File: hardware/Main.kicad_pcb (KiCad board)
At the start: 2 copper layers, 54.5 x 57.5 mm, 34 parts, among them Q1 DMG2305UX, SW1 Bourns PEC11R, SW2 Bourns PEC11R, U1 LM386, U2 RDA5807M_Module, U3 RPi_Pico_TH, U4 S-1206B50-M3T1U

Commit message: Revised PCB Layout
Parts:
- AE1: footprint Package_TO_SOT_SMD:SOT-23-3 -> Connector_PinHeader_2.00mm:PinHeader_1x01_P2.00mm_Vertical; moved to F.Cu
- C1: footprint Capacitor_SMD:CP_Elec_8x10 -> Capacitor_Tantalum_SMD:CP_EIA-7343-30_AVX-N
- RV1: value R_Potentiometer_Trim_US -> 10kΩ
- moved LS1 52.1 mm to (165.0, 72.0), turned to 90 degrees
- moved AE1 42.8 mm to (142.5, 71.0), turned to 0 degrees
- moved C1 41.0 mm to (166.0, 76.0)
- moved C2 40.9 mm to (168.5, 81.5)
- moved C8 36.4 mm to (144.0, 109.9)
- moved R10 36.4 mm to (148.5, 109.8)
- moved R12 36.4 mm to (153.0, 109.9)
- moved R1 32.7 mm to (168.5, 87.9), turned to -90 degrees
- moved C6 27.9 mm to (144.0, 122.8)
- moved R6 27.9 mm to (148.5, 122.7)
- moved R8 27.9 mm to (153.0, 122.9)
- moved C3 25.6 mm to (159.6, 85.2), turned to 0 degrees
- moved C4 25.0 mm to (151.0, 86.5)
- moved R2 25.0 mm to (150.6, 90.5)
- moved R3 25.0 mm to (144.5, 93.0)
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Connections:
- RV1 pad 1: Net-(C4-Pad1) -> GND
- RV1 pad 2: GND -> Net-(U2-ROUT)
- RV1 pad 3: Net-(U2-ROUT) -> Net-(C4-Pad1)
- U3 pad 1: /ENC2A -> unconnected-(U3-GP0-Pad1)
- U3 pad 10: /DISP_DC -> unconnected-(U3-GP7-Pad10)
- U3 pad 15: unconnected-(U3-GP11-Pad15) -> /DISP_RES
- U3 pad 16: unconnected-(U3-GP12-Pad16) -> /DISP_DC
- U3 pad 17: unconnected-(U3-GP13-Pad17) -> /DISP_CS
- U3 pad 19: /ENC1A -> /DISP_SCLK
- U3 pad 2: /ENC2B -> unconnected-(U3-GP1-Pad2)
- U3 pad 20: /ENC1B -> /DISP_SDA
- U3 pad 21: /Radio-Audio/Radio_SDA -> /ENC1_BTN
- U3 pad 22: /Radio-Audio/Radio_SCL -> /ENC1A
- U3 pad 24: unconnected-(U3-GP18-Pad24) -> /ENC1B
- U3 pad 26: unconnected-(U3-GP20-Pad26) -> /ENC2_BTN
- U3 pad 27: /ENC1_BTN -> /ENC2A
- U3 pad 29: /ENC2_BTN -> /ENC2B
- U3 pad 31: unconnected-(U3-GP26/ADC0-Pad31) -> /Radio-Audio/Radio_SCL
- U3 pad 32: unconnected-(U3-GP27/ADC1-Pad32) -> /Radio-Audio/Radio_SDA
- U3 pad 4: /DISP_SCLK -> unconnected-(U3-GP2-Pad4)
- U3 pad 5: /DISP_SDA -> unconnected-(U3-GP3-Pad5)
- U3 pad 7: /DISP_CS -> unconnected-(U3-GP5-Pad7)
- U3 pad 9: /DISP_RES -> unconnected-(U3-GP6-Pad9)
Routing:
- net Net-(R6-Pad2): track 0.00 -> 28.0 mm
- net Net-(R10-Pad2): track 0.00 -> 27.9 mm
- net /DISP_RES: track 0.00 -> 27.1 mm
- net /ENC1_BTN: track 0.00 -> 23.4 mm
- net /ENC2_BTN: track 0.00 -> 22.1 mm
- net /DISP_DC: track 0.00 -> 20.0 mm
- net Net-(R11-Pad1): track 0.00 -> 17.0 mm
- net Net-(U1-+): track 0.00 -> 16.9 mm
- net Net-(R5-Pad1): track 0.00 -> 16.1 mm
- net /Radio-Audio/Radio_SCL: track 0.00 -> 14.3 mm
- net /DISP_CS: track 0.00 -> 14.0 mm
- net /DISP_SCLK: track 0.00 -> 13.5 mm
- net /Radio-Audio/Radio_SDA: track 0.00 -> 12.8 mm
- net Net-(AE1-A): track 0.00 -> 12.3 mm
- net /ENC2B: track 0.00 -> 12.2 mm
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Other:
- board size 54.5 x 57.5 mm -> 52 x 57 mm

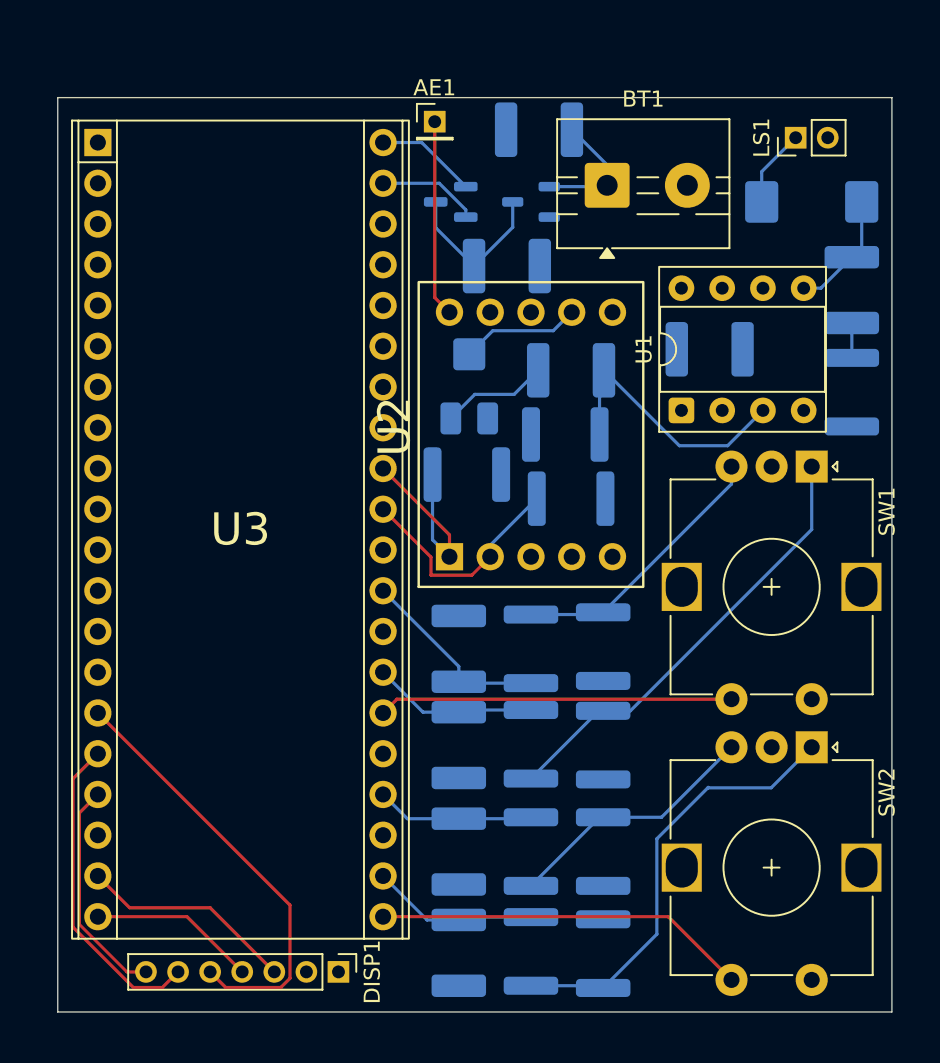
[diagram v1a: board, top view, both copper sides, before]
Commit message: Reduced Component Sizes + Added Mounting Holes
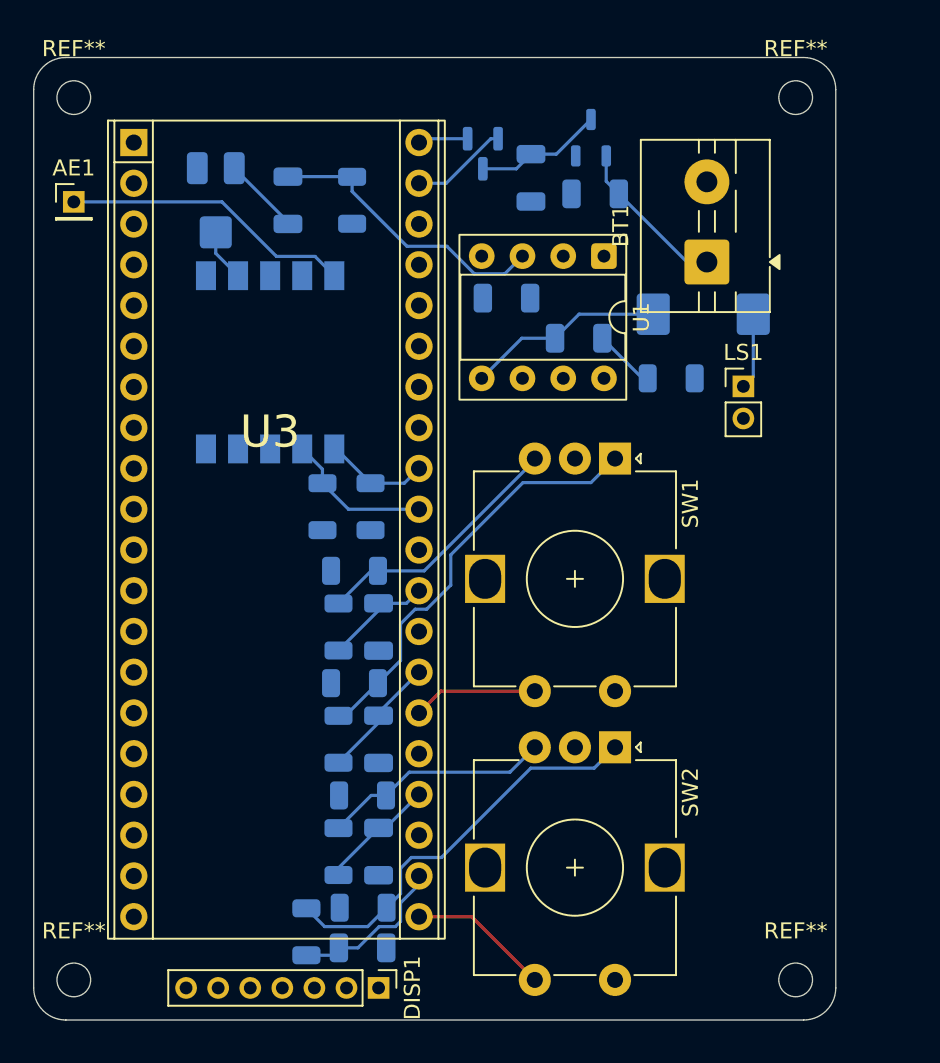
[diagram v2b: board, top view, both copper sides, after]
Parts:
- added REF**: MountingHole_2.1mm, MountingHole:MountingHole_2.1mm, F.Cu at (120.0, 124.5)
- added REF**: MountingHole_2.1mm, MountingHole:MountingHole_2.1mm, F.Cu at (120.0, 69.5)
- added REF**: MountingHole_2.1mm, MountingHole:MountingHole_2.1mm, F.Cu at (165.0, 69.5)
- added REF**: MountingHole_2.1mm, MountingHole:MountingHole_2.1mm, F.Cu at (165.0, 124.5)
- C10, C2, C3, C4, C5, C6, C7, C8, C9: footprint Capacitor_SMD:C_1812_4532Metric -> Capacitor_SMD:C_1206_3216Metric
- R1, R10, R11, R12, R2, R3, R4, R5, R6, R7, R8, R9: footprint Resistor_SMD:R_1812_4532Metric -> Resistor_SMD:R_1206_3216Metric
- U2: footprint ECE:RDA5807M_Module_TH -> ECE:RDA5807M_Module_SM; moved to B.Cu
- moved AE1 23.0 mm to (120.0, 76.0)
- moved C4 20.6 mm to (133.3, 75.9), turned to 90 degrees
- moved R2 19.7 mm to (137.3, 75.9), turned to -90 degrees
- moved RV1 19.6 mm to (128.8, 75.9), turned to 180 degrees
- moved C2 17.3 mm to (151.5, 84.5), turned to 0 degrees
- moved U2 16.9 mm to (132.2, 86.0)
- moved R11 16.2 mm to (137.5, 99.0), turned to 180 degrees
- moved R12 16.0 mm to (137.5, 106.0), turned to 180 degrees
- moved LS1 15.8 mm to (161.7, 87.5), turned to 0 degrees
- moved R4 15.5 mm to (135.5, 95.0), turned to 90 degrees
- moved R7 15.4 mm to (138.0, 113.0), turned to 180 degrees
- moved R8 15.2 mm to (138.0, 120.0), turned to 180 degrees
- moved R6 14.1 mm to (134.5, 121.5), turned to 90 degrees
- moved C3 13.1 mm to (147.0, 82.0), turned to 180 degrees
- moved SW1 12.3 mm to (153.7, 92.0)
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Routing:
- net /DISP_RES: track 27.1 -> 0.00 mm
- net /DISP_DC: track 20.0 -> 0.00 mm
- net /ENC1_BTN: track 23.4 -> 8.85 mm
- net /ENC2_BTN: track 22.1 -> 7.78 mm
- net /DISP_CS: track 14.0 -> 0.00 mm
- net /DISP_SCLK: track 13.5 -> 0.00 mm
- net /DISP_SDA: track 10.4 -> 0.00 mm
- net /Radio-Audio/Radio_SDA: track 12.8 -> 6.55 mm
- net Net-(AE1-A): track 12.3 -> 18.1 mm
- net /ENC2B: track 12.2 -> 6.82 mm
- net /Radio-Audio/Radio_SCL: track 14.3 -> 9.35 mm
- net Net-(C1-Pad1): track 7.51 -> 12.3 mm
- net Net-(U2-ROUT): track 7.48 -> 3.28 mm
- net /Power/VBUS: track 6.30 -> 3.13 mm
- net Net-(R6-Pad2): track 28.0 -> 25.3 mm
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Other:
- board size 52 x 57 mm -> 50 x 60 mm

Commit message: Repositioned + Added volume potentiometer to PMW Audio
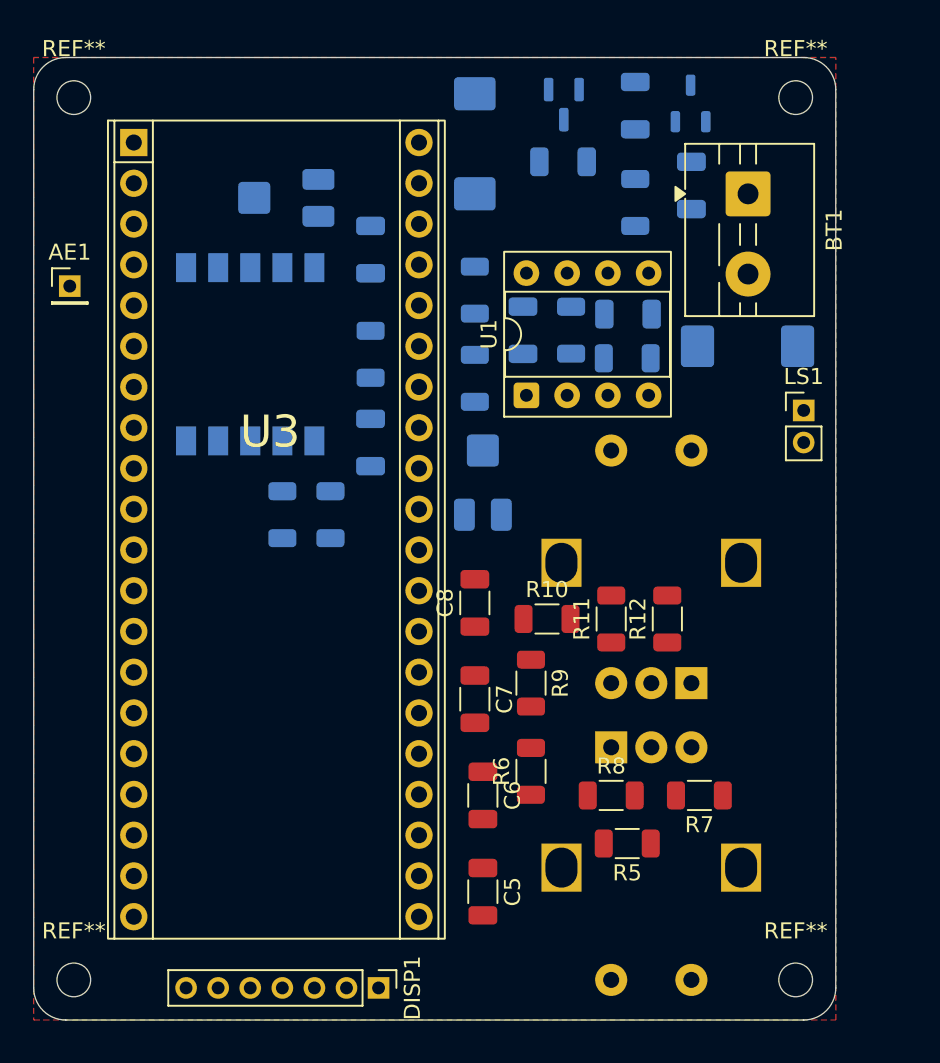
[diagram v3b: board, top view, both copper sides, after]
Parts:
- removed U2: RDA5807M_Module, ECE:RDA5807M_Module_SM
- added C11: 100nF, Capacitor_SMD:C_1206_3216Metric, B.Cu at (148.0, 84.0)
- added C12: 47uF, Capacitor_SMD:C_1206_3216Metric, B.Cu at (138.5, 91.0)
- added C13: 470 uF, Capacitor_Tantalum_SMD:CP_EIA-7343-30_AVX-N, B.Cu at (145.0, 72.4)
- added R13: 220, Resistor_SMD:R_1206_3216Metric, B.Cu at (138.5, 85.5)
- added R14: 100, Resistor_SMD:R_1206_3216Metric, B.Cu at (145.0, 81.5)
- added R15: 1.8k, Resistor_SMD:R_1206_3216Metric, B.Cu at (145.0, 87.0)
- added R16: No fit, Resistor_SMD:R_1206_3216Metric, B.Cu at (154.5, 85.8)
- added RV2: 10kΩ, Potentiometer_SMD:Potentiometer_Bourns_3314J_Vertical, B.Cu at (145.5, 93.5)
- added U5: RDA5807M_Module, ECE:RDA5807M_Module_SM, B.Cu at (131.0, 85.5)
- C5, C6, C7, C8, R10, R11, R12, R5, R6, R7, R8, R9: moved to F.Cu
- SW1, SW2: moved to B.Cu
- moved R7 21.0 mm to (159.0, 113.0)
- moved R12 19.9 mm to (157.0, 102.0), turned to 90 degrees
- moved R5 18.0 mm to (154.5, 116.0), turned to 180 degrees
- moved R6 17.2 mm to (148.5, 111.5)
- moved R8 17.0 mm to (153.5, 113.0), turned to 0 degrees
- moved R11 16.3 mm to (153.5, 102.0), turned to 90 degrees
- moved R2 15.9 mm to (151.0, 84.0), turned to 90 degrees
- moved R10 15.0 mm to (149.5, 102.0), turned to 0 degrees
- moved SW1 14.8 mm to (158.5, 106.0), turned to 90 degrees
- moved R9 12.5 mm to (148.5, 106.0)
- moved C6 12.1 mm to (145.5, 113.0), turned to -90 degrees
- moved R1 11.2 mm to (155.0, 76.0), turned to 90 degrees
- moved C8 10.4 mm to (145.0, 101.0), turned to 90 degrees
- moved U1 9.94 mm to (148.2, 88.1), turned to 90 degrees
- moved C3 9.20 mm to (150.5, 73.5)
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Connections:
- U3 pad 22: /ENC1A -> /ENC1B
- U3 pad 24: /ENC1B -> /ENC1A
- U3 pad 26: /ENC2_BTN -> /ENC2B
- U3 pad 29: /ENC2B -> /ENC2_BTN
- U3 pad 34: unconnected-(U3-GP28/ADC2-Pad34) -> /Radio-Audio/PWM Audio
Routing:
- net Net-(R10-Pad2): track 26.3 -> 0.00 mm
- net Net-(R6-Pad2): track 25.3 -> 0.00 mm
- net Net-(AE1-A): track 18.1 -> 0.00 mm
- net Net-(U1-+): track 18.1 -> 0.00 mm
- net Net-(R11-Pad1): track 16.0 -> 0.00 mm
- net Net-(R5-Pad1): track 14.3 -> 0.00 mm
- net Net-(C1-Pad1): track 12.3 -> 0.00 mm
- net /ENC1A: track 10.1 -> 0.00 mm
- net Net-(BT1-+): track 9.94 -> 0.00 mm
- net /Radio-Audio/Radio_SCL: track 9.35 -> 0.00 mm
- net /ENC1_BTN: track 8.85 -> 0.00 mm
- net Net-(Q1-D): track 8.01 -> 0.00 mm
- net /ENC2_BTN: track 7.78 -> 0.00 mm
- net /ENC2A: track 7.72 -> 0.00 mm
- net /ENC1B: track 7.36 -> 0.00 mm
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- added copper zone on F.Cu, net GND

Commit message: Did it all lmao (pcb traces ready for full review)
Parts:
- added R17: 0 ohm, Resistor_SMD:R_1206_3216Metric, B.Cu at (137.2, 81.0)
- added R18: 0 ohm, Resistor_SMD:R_1206_3216Metric, F.Cu at (120.0, 81.0)
- BT1: value 4.8-6V -> 4 AA
- LS1: footprint Connector_PinHeader_2.00mm:PinHeader_1x02_P2.00mm_Vertical -> TerminalBlock:TerminalBlock_MaiXu_MX126-5.0-02P_1x02_P5.00mm
- R11, R12, R7, R8: moved to B.Cu
- moved R14 36.7 mm to (129.0, 114.5), turned to 0 degrees
- moved C11 33.4 mm to (129.0, 111.5), turned to 0 degrees
- moved R15 29.7 mm to (135.8, 115.2), turned to 0 degrees
- moved C3 27.0 mm to (146.5, 100.2), turned to -90 degrees
- moved R9 26.0 mm to (149.8, 80.0), turned to 0 degrees
- moved C7 25.2 mm to (152.8, 83.0), turned to 180 degrees
- moved R16 25.1 mm to (135.8, 102.5)
- moved R13 24.9 mm to (129.0, 108.5), turned to 180 degrees
- moved R1 24.7 mm to (150.0, 100.2), turned to -90 degrees
- moved C12 21.7 mm to (135.8, 112.5), turned to 180 degrees
- moved R11 20.8 mm to (145.0, 83.0), turned to -90 degrees
- moved SW1 20.7 mm to (148.2, 88.0), turned to 0 degrees
- moved R12 18.4 mm to (145.0, 88.0)
- moved C2 17.3 mm to (153.0, 100.2), turned to -90 degrees
- moved RV2 17.1 mm to (135.8, 107.5), turned to 180 degrees
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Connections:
- C4 pad 2: Net-(U1-+) -> Net-(C4-Pad2)
- R2 pad 1: Net-(U1-+) -> Net-(C4-Pad2)
- U3 pad 11: unconnected-(U3-GP8-Pad11) -> /Radio-Audio/Radio_SDA
- U3 pad 12: unconnected-(U3-GP9-Pad12) -> /Radio-Audio/Radio_SCL
- U3 pad 14: unconnected-(U3-GP10-Pad14) -> /Radio-Audio/PWM Audio
- U3 pad 26: /ENC2B -> unconnected-(U3-GP20-Pad26)
- U3 pad 27: /ENC2A -> unconnected-(U3-GP21-Pad27)
- U3 pad 29: /ENC2_BTN -> unconnected-(U3-GP22-Pad29)
- U3 pad 31: /Radio-Audio/Radio_SCL -> /ENC2B
- U3 pad 32: /Radio-Audio/Radio_SDA -> /ENC2A
- U3 pad 34: /Radio-Audio/PWM Audio -> /ENC2_BTN
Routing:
- net +3.3V: track 0.00 -> 73.0 mm, vias 0 -> 4
- net Net-(U1-+): track 0.00 -> 51.5 mm
- net GND: track 0.00 -> 46.8 mm, vias 0 -> 14
- net +5V: track 0.00 -> 46.3 mm
- net Net-(AE1-A): track 0.00 -> 32.9 mm
- net /ENC1_BTN: track 0.00 -> 29.0 mm
- net /ENC2B: track 0.00 -> 27.3 mm
- net /ENC2_BTN: track 0.00 -> 25.5 mm
- net /Radio-Audio/Radio_SDA: track 0.00 -> 23.6 mm
- net /ENC1B: track 0.00 -> 22.7 mm
- net /ENC1A: track 0.00 -> 22.2 mm, vias 0 -> 1
- net /DISP_RES: track 0.00 -> 19.5 mm
- net /DISP_DC: track 0.00 -> 16.2 mm
- net Net-(BT1-+): track 0.00 -> 14.9 mm
- net /ENC2A: track 0.00 -> 14.6 mm
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- added copper zone on F.Cu, net /Radio-Audio/Board Antenna
- added copper zone on B.Cu, net GND

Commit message: done for real this time
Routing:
- net GND: track 46.8 -> 45.1 mm
- net +5V: track 46.3 -> 47.8 mm
- net Net-(Q1-D): track 12.3 -> 11.3 mm

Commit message: PCB tweaks
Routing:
- net /ENC2B: track 27.3 -> 32.6 mm
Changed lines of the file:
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@@
 		(tags "resistor")
 		(property "Reference" "R18"
-			(at 0 -1.83 90)
+			(at 3.0625 0 180)
 			(layer "F.SilkS")
 			(effects
@@
 		)
 		(property "Value" "0.01uF"
-			(at 0 1.85 0)
+			(at -5.05 0 0)
 			(layer "F.Fab")
 			(effects
@@
 			(at 0 -3.05 0)
 			(layer "F.SilkS")
+			(hide yes)
 			(effects
 				(font
@@
 		)
 		(property "Value" "10kΩ"
-			(at 0 1.83 0)
+			(at 4.15 -0.1 0)
 			(layer "F.Fab")
 			(effects
@@
 			(at 0 -3.05 0)
 			(layer "F.SilkS")
+			(hide yes)
 			(effects
 				(font
@@
 			(at 2.24 3.05 0)
 			(layer "F.Fab")
+			(hide yes)
 			(effects
 				(font
@@
 			(layer "F.CrtYd")
 		)
-		(fp_text user "${REFERENCE}"
-			(at 0 0 0)
-			(layer "F.Fab")
-			(effects
-				(font
-					(size 1 1)
-					(thickness 0.15)
-				)
-			)
-		)
 		(pad "" np_thru_hole circle
 			(at 0 0)
@@
 		)
 		(property "Value" "10kΩ"
-			(at 0 1.83 0)
+			(at -4.15 -0.1 0)
 			(layer "F.Fab")
 			(effects
@@
 		(tags "Through hole pin header THT 1x07 2.00mm single row")
 		(property "Reference" "DISP1"
-			(at 0 -2.11 90)
+			(at 0 -3.75 180)
 			(layer "F.SilkS")
 			(effects
@@
 		(tags "mountinghole")
 		(property "Reference" "REF**"
-			(at 0 -3.05 0)
+			(at -0.4 4.5 0)
 			(layer "F.SilkS")
+			(hide yes)
 			(effects
 				(font
@@
 		)
 		(property "Value" "MountingHole_2.1mm"
-			(at 2.24 3.05 0)
+			(at 11.3 6.9 0)
 			(layer "F.Fab")
+			(hide yes)
 			(effects
 				(font
@@
 			(layer "F.CrtYd")
 		)
-		(fp_text user "${REFERENCE}"
-			(at 0 0 0)
-			(layer "F.Fab")
-			(effects
-				(font
-					(size 1 1)
-					(thickness 0.15)
-				)
-			)
-		)
 		(pad "" np_thru_hole circle
 			(at 0 0)
@@
 		(tags "THT terminal block MaiXu MX126-5.0-02P pitch 5mm size 10.5x7.8mm drill 1.3mm pad 2.8mm")
 		(property "Reference" "LS1"
-			(at 2.25 -5.12 90)
+			(at -4.05 0.0325 180)
 			(layer "F.SilkS")
 			(effects
@@
 			(at 0 -3.05 0)
 			(layer "F.SilkS")
+			(hide yes)
 			(effects
 				(font
@@
 		)
 		(property "Value" "0.01uF"
-			(at 0 1.85 0)
+			(at -4.65 -0.1 0)
 			(layer "F.Fab")
 			(effects
@@
 			(at 9.64619 -2.4 0)
 			(layer "F.Fab")
+			(hide yes)
 			(effects
 				(font
@@
 	)
 	(segment
+		(start 128.85 115.8125)
+		(end 127.5375 114.5)
+		(width 0.35)
+		(layer "B.Cu")
+		(net 3)
+	)
+	(segment
 		(start 146.8875 72.7)
 		(end 148.05 72.7)
@@
 	)
 	(segment
-		(start 134.2875 115.25)
-		(end 133.725 115.8125)
+		(start 133.725 115.8125)
+		(end 128.85 115.8125)
 		(width 0.35)
 		(layer "B.Cu")
@@
 	)
 	(segment
-		(start 128.85 115.8125)
-		(end 127.5375 114.5)
-		(width 0.35)
-		(layer "B.Cu")
-		(net 3)
-	)
-	(segment
 		(start 129.025 107.475)
 		(end 128.55 107)
@@
 	)
 	(segment
+		(start 134.2875 115.25)
+		(end 133.725 115.8125)
+		(width 0.35)
+		(layer "B.Cu")
+		(net 3)
+	)
+	(segment
 		(start 140.275 69.5)
 		(end 139.225 69.5)
@@
 	)
 	(segment
-		(start 133.725 115.8125)
-		(end 128.85 115.8125)
-		(width 0.35)
-		(layer "B.Cu")
-		(net 3)
-	)
-	(segment
 		(start 137.85 105.5)
 		(end 137.9 105.45)
@@
 	)
 	(segment
-		(start 151.2125 80)
-		(end 154.2125 83)
+		(start 157.8 92.402)
+		(end 155.042 95.16)
 		(width 0.2)
 		(layer "F.Cu")
@@
 	)
 	(segment
-		(start 153.66484 89.201)
-		(end 153.66484 90.27132)
+		(start 151.2125 80)
+		(end 154.2125 83)
 		(width 0.2)
 		(layer "F.Cu")
@@
 	)
 	(segment
-		(start 155.101 88.88516)
-		(end 154.78516 89.201)
+		(start 157.8 86.575)
+		(end 157.8 92.402)
 		(width 0.2)
 		(layer "F.Cu")
@@
 	)
 	(segment
-		(start 148.77616 95.16)
+		(start 155.042 95.16)
 		(end 141.52 95.16)
 		(width 0.2)
@@
 	(segment
 		(start 154.225 83)
-		(end 155.101 83.876)
-		(width 0.2)
-		(layer "F.Cu")
-		(net 12)
-	)
-	(segment
-		(start 153.66484 90.27132)
-		(end 148.77616 95.16)
-		(width 0.2)
-		(layer "F.Cu")
-		(net 12)
-	)
-	(segment
-		(start 154.78516 89.201)
-		(end 153.66484 89.201)
-		(width 0.2)
-		(layer "F.Cu")
-		(net 12)
-	)
-	(segment
-		(start 155.101 83.876)
-		(end 155.101 88.88516)
+		(end 157.8 86.575)
 		(width 0.2)
 		(layer "F.Cu")
@@
 	)
 	(zone
+		(net 0)
+		(net_name "")
+		(layer "F.Cu")
+		(hatch edge 0.5)
+		(connect_pads
+			(clearance 0)
+		)
+		(min_thickness 0.25)
+		(filled_areas_thickness no)
+		(keepout
+			(tracks allowed)
+			(vias allowed)
+			(pads allowed)
+			(copperpour not_allowed)
+			(footprints allowed)
+		)
+		(placement
+			(enabled no)
+			(sheetname "")
+		)
+		(fill
+			(thermal_gap 0.5)
+			(thermal_bridge_width 0.5)
+		)
+		(polygon
+			(pts
+				(xy 142.6 93.1) (xy 154.2 89.3) (xy 154.2 92.4) (xy 156.8 92.4) (xy 154.9 94.6) (xy 142.6 94.6)
+			)
+		)
+	)
+	(zone
